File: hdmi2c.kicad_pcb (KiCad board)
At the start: 2 copper layers, 95 x 45 mm, 61 parts, among them J1 USB_C_Receptacle_USB2.0, J7 HDMI1, J8 HDMI2, M1 MountingHole_2.2mm_M2_DIN965_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, M2 MountingHole_2.2mm_M2_DIN965_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, M3 MountingHole_2.2mm_M2_DIN965_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, M4 MountingHole_2.2mm_M2_DIN965_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, Q1 Q_NPN_BEC, Q2 Q_NPN_BEC, Q3 BSS138, Q4 BSS138, Q5 BSS138, Q6 BSS138, Q7 BSS83P, Q8 BSS83P, SW1 reset_sw, SW2 SW_Push_shell, SW3 SW_Push_shell, U1 CP2102N-Axx-xQFN24, U3 ESP32-WROOM-32, U4 MIC5205-5.0YM5, U5 MIC5205-5.0YM5, U6 MIC5504-3.3YM5

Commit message: Add project configuration files and initial scripts for HDMI2C development
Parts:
- removed C6: 2.2uF, Capacitor_SMD:C_0603_1608Metric
- removed J8: HDMI2, hdmi2c:WURTH_685119134923_HDMI
- removed JP2: HDMI2_SH_GND, Jumper:SolderJumper-2_P1.3mm_Open_RoundedPad1.0x1.5mm
- removed JP7: HDMI2_SCL, Jumper:SolderJumper-2_P1.3mm_Bridged_RoundedPad1.0x1.5mm
- removed JP8: HDMI2_SDA, Jumper:SolderJumper-2_P1.3mm_Bridged_RoundedPad1.0x1.5mm
- removed Q4, Q6: BSS138, Package_TO_SOT_SMD:SOT-23
- removed Q8: BSS83P, Package_TO_SOT_SMD:SOT-23
- removed R10, R8: 10k, Resistor_SMD:R_0603_1608Metric
- removed R12, R14: 2k, Resistor_SMD:R_0603_1608Metric
- removed R20: 2.2k, Resistor_SMD:R_0603_1608Metric
- removed R21: 3.3k, Resistor_SMD:R_0603_1608Metric
- removed U5: MIC5205-5.0YM5, Package_TO_SOT_SMD:SOT-23-5
- moved svg2mod 58.0 mm to (70.0, 42.6)
- moved M1 25.0 mm to (128.0, 83.2)
- moved M2 25.0 mm to (128.0, 44.6)
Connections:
- U3 pad 28: /HDMI2_HPD_3.3 -> unconnected-(U3-IO17-Pad28)
- U3 pad 31: /HDMI2_5V_EN -> unconnected-(U3-IO19-Pad31)
- U3 pad 8: /I2C2_SCL -> unconnected-(U3-IO32-Pad8)
- U3 pad 9: /I2C2_SDA -> unconnected-(U3-IO33-Pad9)
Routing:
- net /I2C2_SCL: track 77.8 -> 0.00 mm, vias 2 -> 0
- net /I2C2_SDA: track 69.3 -> 0.00 mm
- net /HDMI2_5V_EN: track 61.6 -> 0.00 mm, vias 2 -> 0
- net Net-(J8-Pad19): track 38.8 -> 0.00 mm, vias 2 -> 0
- net /HDMI2_HPD_3.3: track 35.5 -> 0.00 mm, vias 2 -> 0
- net +3V3: track 129.0 -> 97.8 mm
- net Net-(J8-PadSH): track 30.4 -> 0.00 mm
- net VBUS: track 89.5 -> 60.7 mm
- net /HDMI2_5V: track 16.2 -> 0.00 mm, vias 2 -> 0
- net /HDMI2_SCL: track 14.4 -> 0.00 mm
- net GND: track 69.3 -> 56.2 mm, vias 19 -> 15
- net /HDMI2_SDA: track 11.8 -> 0.00 mm
- net /HDMI2_SDA_3.3: track 6.50 -> 0.00 mm
- net /HDMI2_SCL_3.3: track 6.46 -> 0.00 mm
- net Net-(C6-Pad1): track 4.37 -> 0.00 mm
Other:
- board size 95 x 45 mm -> 70 x 45 mm

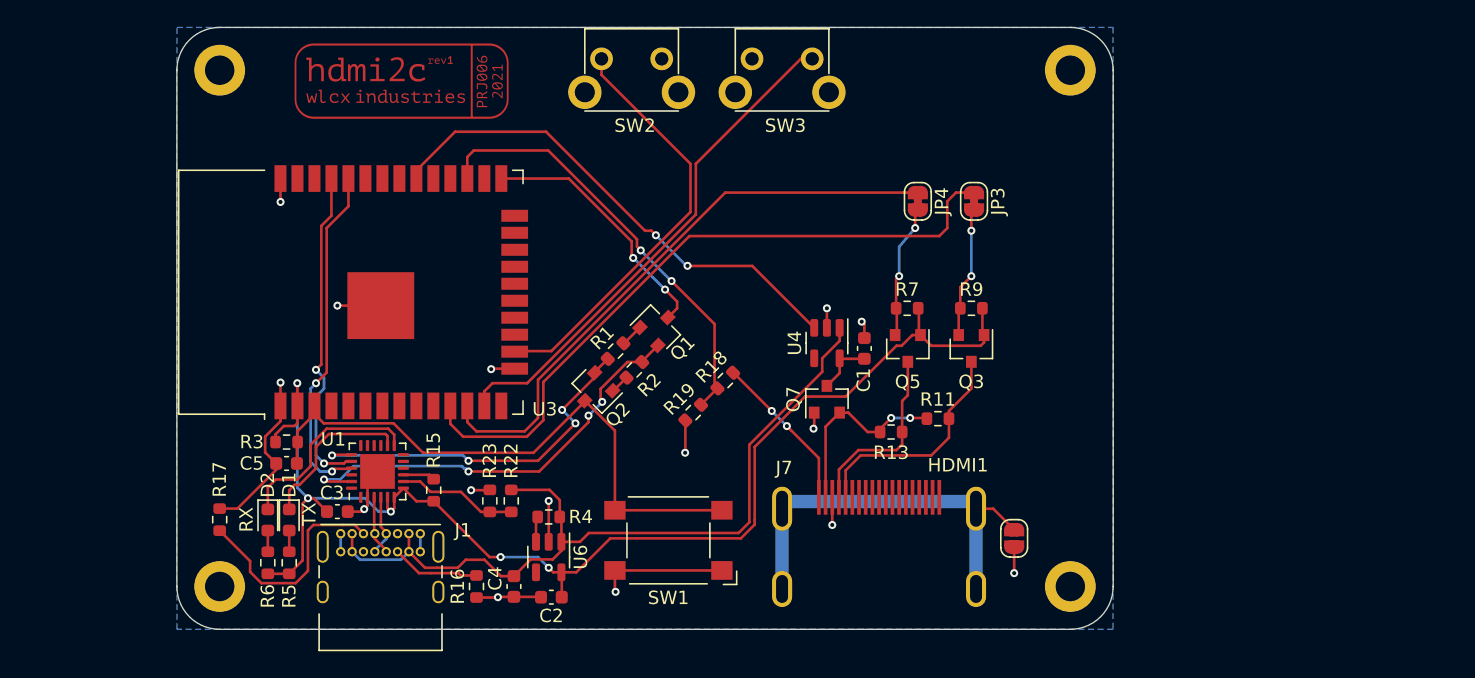
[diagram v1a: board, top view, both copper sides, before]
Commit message: Add rev2 prototype files and update design parameters for HDMI2C carrier
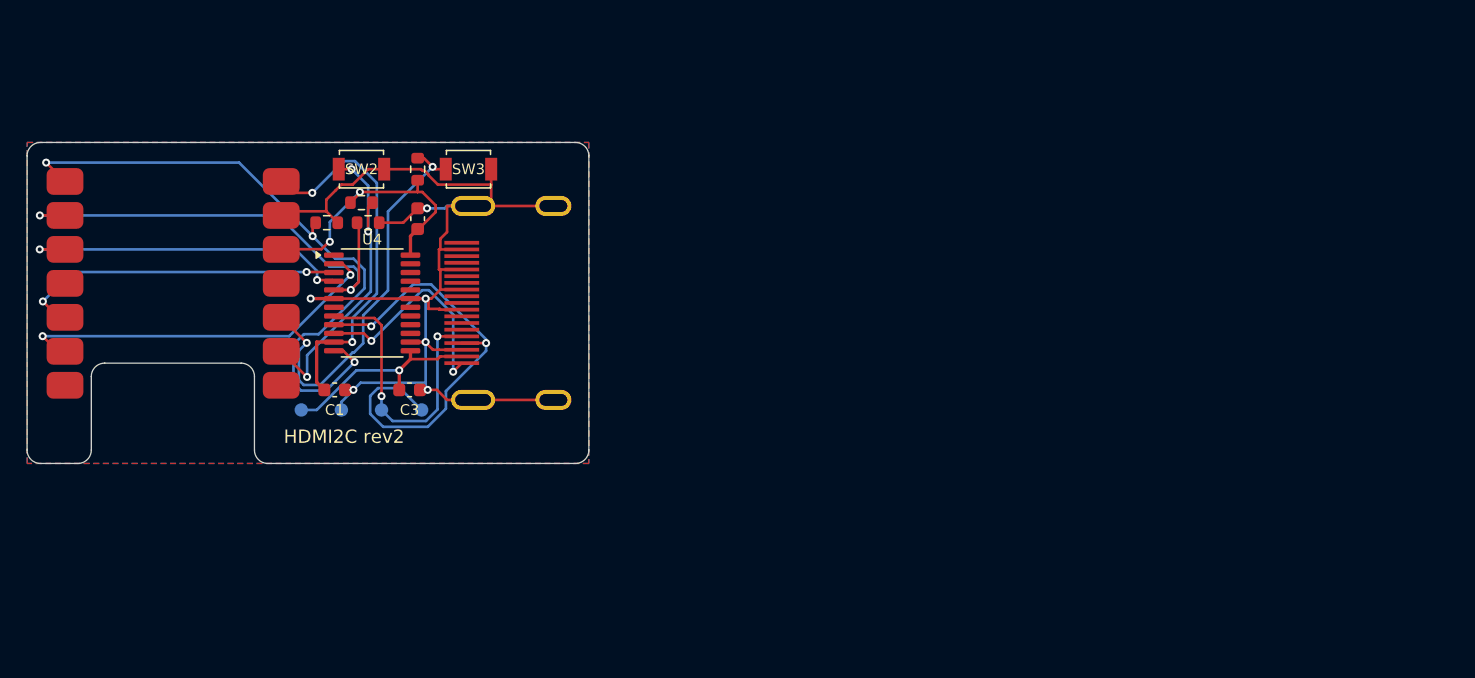
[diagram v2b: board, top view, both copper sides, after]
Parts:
- removed C4: 10uF, Capacitor_SMD:C_0603_1608Metric
- removed C5: 1uF, Capacitor_SMD:C_0603_1608Metric
- removed D1: TX, LED_SMD:LED_0603_1608Metric
- removed D2: RX, LED_SMD:LED_0603_1608Metric
- removed J1: USB_C_Receptacle_USB2.0, Connector_USB:USB_C_Receptacle_GCT_USB4085
- removed JP1: HDMI1_SH_GND, Jumper:SolderJumper-2_P1.3mm_Open_RoundedPad1.0x1.5mm
- removed JP3: HDMI1_SCL, Jumper:SolderJumper-2_P1.3mm_Bridged_RoundedPad1.0x1.5mm
- removed JP4: HDMI1_SDA, Jumper:SolderJumper-2_P1.3mm_Bridged_RoundedPad1.0x1.5mm
- removed M1, M2, M3, M4: MountingHole_2.2mm_M2_DIN965_Pad_with_paste, hdmi2c:MountingHole_2.2mm_M2_DIN965_Pad_with_paste
- removed Q1, Q2: Q_NPN_BEC, Package_TO_SOT_SMD:SOT-23
- removed Q3, Q5: BSS138, Package_TO_SOT_SMD:SOT-23
- removed Q7: BSS83P, Package_TO_SOT_SMD:SOT-23
- removed R1, R2, R3, R7, R9: 10k, Resistor_SMD:R_0603_1608Metric
- removed R11, R13: 2k, Resistor_SMD:R_0603_1608Metric
- removed R15: 1k, Resistor_SMD:R_0603_1608Metric
- removed R16, R17: 5.1k, Resistor_SMD:R_0603_1608Metric
- removed R18: 2.2k, Resistor_SMD:R_0603_1608Metric
- removed R19: 3.3k, Resistor_SMD:R_0603_1608Metric
- removed R22: 22k, Resistor_SMD:R_0603_1608Metric
- removed R23: 47k, Resistor_SMD:R_0603_1608Metric
- removed R4: 100k, Resistor_SMD:R_0603_1608Metric
- removed R5, R6: 68R, Resistor_SMD:R_0603_1608Metric
- removed SW1: reset_sw, Button_Switch_SMD:SW_SPST_Omron_B3FS-101xP
- removed U1: CP2102N-Axx-xQFN24, Package_DFN_QFN:QFN-24-1EP_4x4mm_P0.5mm_EP2.6x2.6mm
- removed U6: MIC5504-3.3YM5, Package_TO_SOT_SMD:SOT-23-5
- removed svg2mod: G***, hdmi2c:logo
- added R24: 100k, Resistor_SMD:R_0603_1608Metric, F.Cu at (72.4, 56.0)
- added R25: 100k, Resistor_SMD:R_0603_1608Metric, F.Cu at (75.5, 56.0)
- added R26: 10k, Resistor_SMD:R_0603_1608Metric, F.Cu at (75.0, 54.5)
- added R27: 10k, Resistor_SMD:R_0603_1608Metric, F.Cu at (79.2, 52.0)
- added TP1: HDMI_5V, TestPoint:TestPoint_Pad_D1.0mm, B.Cu at (70.5, 70.0)
- added TP2: GND, TestPoint:TestPoint_Pad_D1.0mm, B.Cu at (73.5, 70.0)
- added TP3: SCL_5V, TestPoint:TestPoint_Pad_D1.0mm, B.Cu at (76.5, 70.0)
- added TP4: SDA_5V, TestPoint:TestPoint_Pad_D1.0mm, B.Cu at (79.5, 70.0)
- C1: value 2.2uF -> 100nF
- C2, C3: value 1uF -> 100nF
- SW2, SW3: value SW_Push_shell -> B3U-1000P; footprint hdmi2c:SW_TH_Tactile_Omron_B3F-312x -> Button_Switch_SMD:SW_SPST_B3U-1000P
- U3: value ESP32-WROOM-32 -> XIAO ESP32-C6; footprint RF_Module:ESP32-WROOM-32 -> hdmi2c:XIAO_ESP32C6_Castellated
- U4: value MIC5205-5.0YM5 -> TPD12S016PWR; footprint Package_TO_SOT_SMD:SOT-23-5 -> Package_SO:TSSOP-24_4.4x7.8mm_P0.65mm
- moved C1 39.7 mm to (73.0, 68.5), turned to 0 degrees
- moved J7 34.4 mm to (82.5, 62.0), turned to 90 degrees
- moved U4 34.1 mm to (75.8, 62.0), turned to 0 degrees
- moved C2 30.0 mm to (79.2, 55.7), turned to 90 degrees
- moved SW3 27.6 mm to (83.0, 52.0), turned to 0 degrees
- moved U3 27.1 mm to (52.0, 71.0), turned to 0 degrees
- moved SW2 24.4 mm to (75.0, 52.0), turned to 0 degrees
- moved C3 10.6 mm to (78.6, 68.5), turned to 0 degrees
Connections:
- C1 pad 1: Net-(C1-Pad1) -> /VBUS
- C1 pad 2: GND -> /GND
- C2 pad 1: +3V3 -> /+3V3
- C2 pad 2: GND -> /GND
- C3 pad 1: GND -> /HDMI_5V
- C3 pad 2: +3V3 -> /GND
- J7 pad 11: /HDMI1_CKS -> /GND
- J7 pad 13: /HDMI1_CEC -> unconnected-(J7-CEC-Pad13)
- J7 pad 15: /HDMI1_SCL -> /HDMI_SCL
- J7 pad 16: /HDMI1_SDA -> /HDMI_SDA
- J7 pad 17: GND -> /GND
- J7 pad 18: /HDMI1_5V -> /HDMI_5V
- J7 pad 19: Net-(J7-Pad19) -> /HDMI_HPD_5V
- J7 pad 2: /HDMI1_D2S -> /GND
- J7 pad 5: /HDMI1_D1S -> /GND
- J7 pad 8: /HDMI1_D0S -> /GND
- J7 pad SH: Net-(J7-PadSH) -> /GND
- SW2 pad 1: /BUTT1 -> /BUTTON1
- SW2 pad 2: GND -> /GND
- SW3 pad 1: /BUTT2 -> /BUTTON2
- SW3 pad 2: GND -> /GND
- U3 pad 1: GND -> /HDMI_5V_EN
- U3 pad 10: unconnected-(U3-Pad10) -> /BUTTON2
- U3 pad 11: /I2C1_SCL -> unconnected-(U3-D10_/_GPIO18-Pad11)
- U3 pad 12: /I2C1_SDA -> /+3V3
- U3 pad 13: /BUTT2 -> /GND
- U3 pad 14: unconnected-(U3-Pad14) -> /VBUS
- U3 pad 2: +3V3 -> /DDC_EN
- U3 pad 3: /RESET -> /HDMI_HPD
- U3 pad 5: unconnected-(U3-Pad5) -> /I2C_SDA
- U3 pad 6: unconnected-(U3-Pad6) -> /I2C_SCL
- U3 pad 9: unconnected-(U3-IO33-Pad9) -> /BUTTON1
- U4 pad 1: VBUS -> unconnected-(U4-CEC_A-Pad1)
- U4 pad 2: GND -> /I2C_SCL
- U4 pad 3: /HDMI1_5V_EN -> /I2C_SDA
- U4 pad 4: unconnected-(U4-Pad4) -> /HDMI_HPD
- U4 pad 5: Net-(C1-Pad1) -> /DDC_EN
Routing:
- net +3V3: track 97.8 -> 0.00 mm, vias 5 -> 0
- net /GND: track 0.00 -> 92.0 mm, vias 0 -> 6
- net VBUS: track 60.7 -> 0.00 mm
- net GND: track 56.2 -> 0.00 mm, vias 15 -> 0
- net /I2C1_SCL: track 51.3 -> 0.00 mm
- net /HDMI_5V_EN: track 0.00 -> 49.1 mm, vias 0 -> 3
- net /RESET: track 45.7 -> 0.00 mm
- net /I2C1_SDA: track 44.2 -> 0.00 mm
- net /BUTT2: track 38.1 -> 0.00 mm
- net /HDMI1_5V_EN: track 37.6 -> 0.00 mm, vias 2 -> 0
- net /DDC_EN: track 0.00 -> 35.7 mm, vias 0 -> 2
- net /HDMI_SDA: track 0.00 -> 35.4 mm, vias 0 -> 2
- net /BUTT1: track 32.7 -> 0.00 mm
- net /HDMI1_HPD_3.3: track 32.6 -> 0.00 mm, vias 2 -> 0
- net /DTR: track 32.6 -> 0.00 mm, vias 4 -> 0
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- added copper zone on B.Cu, net /GND
- added copper zone on F.Cu, net /GND
- removed copper zone on B.Cu, net GND
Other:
- board size 70 x 45 mm -> 42 x 24 mm
- board text added: "5V"
- board text added: "Antenna clearance"
- board text added: "D4 SDA / D5 SCL"
- board text added: "DDC control only - no video"
- board text added: "GND"
- board text added: "HDMI2C rev2"
- board text added: "SCL"
- board text added: "SDA"
- board text added: "XIAO ESP32-C6 / USB power"
